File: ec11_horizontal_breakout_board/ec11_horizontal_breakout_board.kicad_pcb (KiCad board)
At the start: 2 copper layers, 12.2 x 9 mm, 6 parts, among them J1 Conn_01x01_Socket, J2 Conn_01x01_Socket, J3 Conn_01x01_Socket, J4 Conn_01x01_Socket, J50 JST-SH-4, SW3 RotaryEncoder_Switch

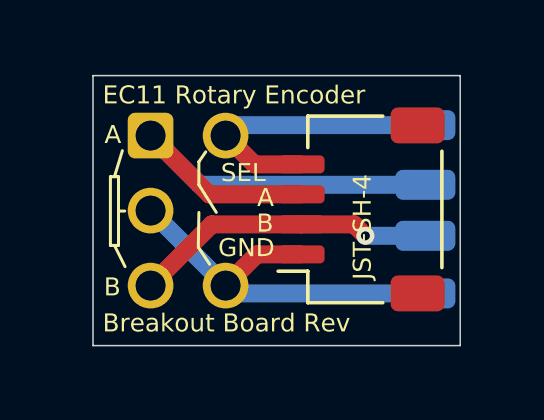
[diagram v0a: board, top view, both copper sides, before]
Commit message: Add filtering to ec11 encoder breakout. Also change to makefile builder
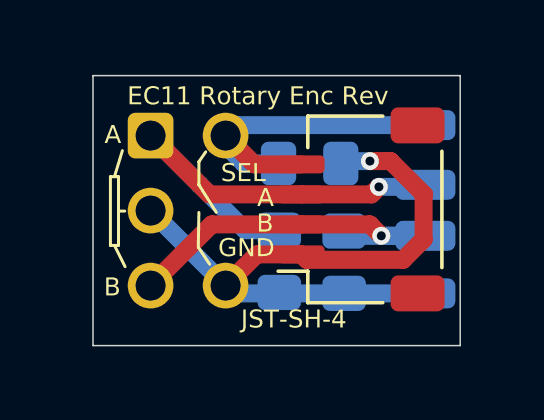
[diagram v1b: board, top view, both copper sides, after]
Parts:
- added C1: 100nF, Capacitor_SMD:C_0805_2012Metric_Pad1.18x1.45mm_HandSolder, B.Cu at (148.4, 101.6)
- added C2: 100nF, Capacitor_SMD:C_0805_2012Metric_Pad1.18x1.45mm_HandSolder, B.Cu at (150.6, 101.6)
- added C3: 100nF, Capacitor_SMD:C_0805_2012Metric_Pad1.18x1.45mm_HandSolder, B.Cu at (149.4, 98.3)
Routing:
- net GND: track 12.9 -> 21.7 mm, vias 0 -> 1
- net /ENC_B: track 9.86 -> 12.9 mm
- net /ENC_PUSH: track 9.44 -> 11.8 mm
- net /ENC_A: track 15.4 -> 15.7 mm, vias 0 -> 1
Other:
- board text added: "100nF"
- board text added: "Cx:0805"
- board text added: "EC11 Rotary Enc Rev${REVISION}"
- board text removed: "Breakout Board Rev${REVISION}"
- board text removed: "EC11 Rotary Encoder"
- board text removed: "ENC_A"
- board text removed: "ENC_B"
- board text removed: "ENC_SEL"

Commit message: Ec11 breakout encoder Rev3
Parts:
- removed C3: 100nF, Capacitor_SMD:C_0805_2012Metric_Pad1.18x1.45mm_HandSolder
- added R1: 1K, EC11:R_0805_2012Metric_Pad1.20x1.40mm_HandSolder_And_Jumper, B.Cu at (149.6, 98.9)
- added R2: 1K, EC11:R_0805_2012Metric_Pad1.20x1.40mm_HandSolder_And_Jumper, B.Cu at (149.6, 100.8)
- moved C1 4.78 mm to (149.7, 97.0), turned to 180 degrees
- moved C2 1.46 mm to (149.7, 102.8), turned to 180 degrees
- moved J1 0.16 mm to (153.1, 102.7)
- moved J2 0.16 mm to (153.1, 100.8)
- moved J4 0.16 mm to (153.1, 97.1)
- moved J3 0.16 mm to (153.1, 99.0)
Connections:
- C1 pad 1: /ENC_A -> /A
- C2 pad 1: /ENC_B -> /B
- J2 pad 1: /ENC_B -> /B
- J3 pad 1: /ENC_A -> /A
- J50 pad 2: /ENC_B -> /B
- J50 pad 3: /ENC_A -> /A
- J50 pad MP: unconnected-(J50-MountPin-PadMP)_1 -> GND
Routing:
- net /ENC_A: track 15.7 -> 5.17 mm, vias 1 -> 0
- net /ENC_B: track 12.9 -> 5.19 mm, vias 1 -> 0
- net /B: track 0.00 -> 7.58 mm, vias 0 -> 1
- net /A: track 0.00 -> 7.58 mm, vias 0 -> 1
- net /ENC_PUSH: track 11.8 -> 7.60 mm, vias 0 -> 1
- net GND: track 21.7 -> 23.3 mm, vias 1 -> 3
- added copper zone on B.Cu, net GND
- added copper zone on F.Cu, net GND
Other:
- board text added: "1KΩ"
